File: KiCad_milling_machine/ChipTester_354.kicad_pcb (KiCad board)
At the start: 2 copper layers, 172 x 61.5 mm, 55 parts, among them U1 TLE2426xP, U2 L7805, U3 TLE2426xP, U4 TLE2426xP, U5 MCP6002-xP

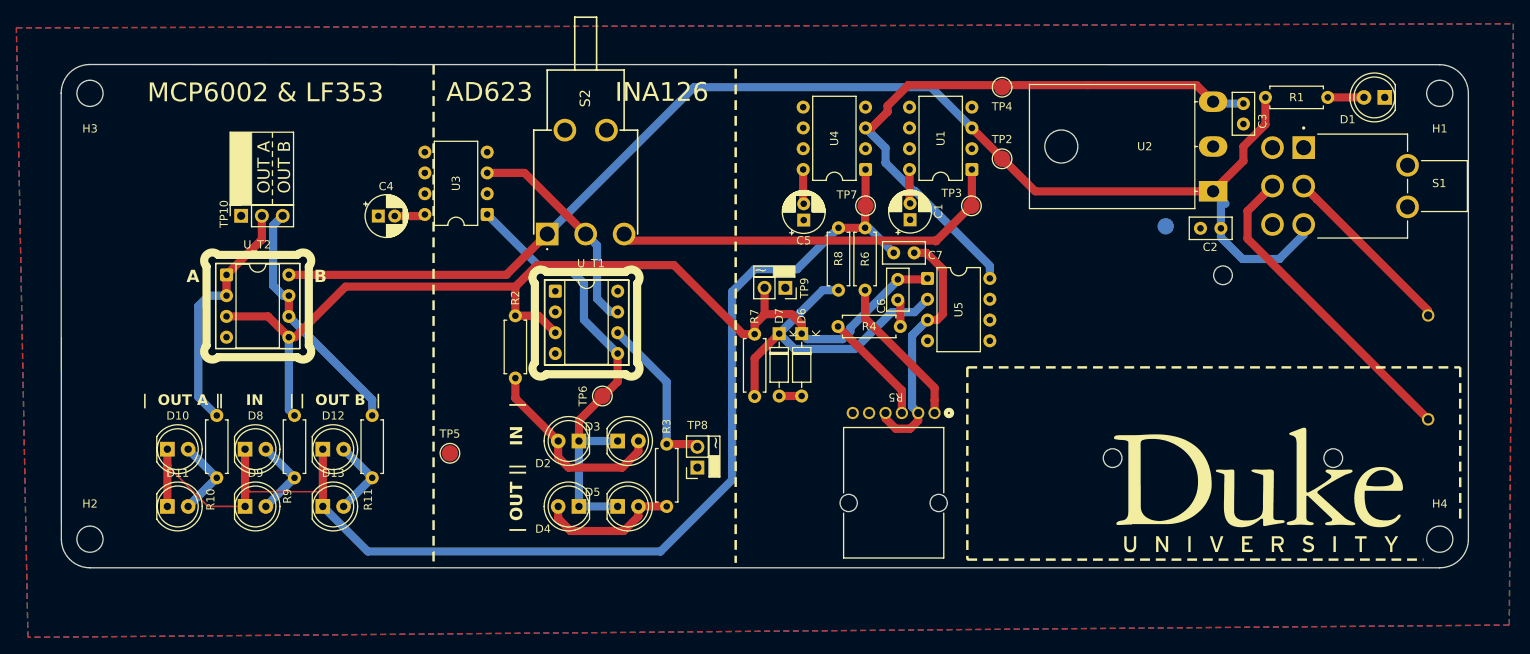
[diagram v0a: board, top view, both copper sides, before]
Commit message: Added milling machine files / updated schematic+pcb annotations /  updated footprints
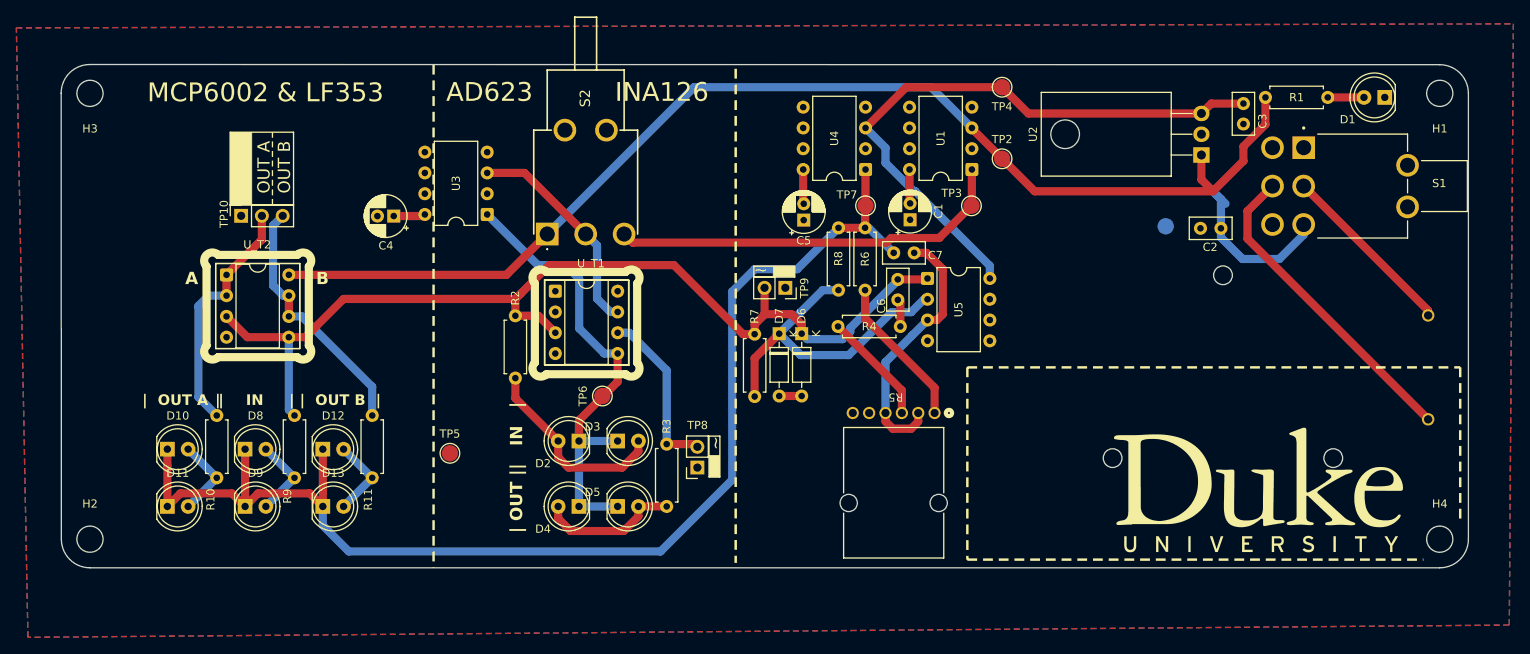
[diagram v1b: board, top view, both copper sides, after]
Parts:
- U2: footprint Package_TO_SOT_THT:TO-218-3_Horizontal_TabDown -> Package_TO_SOT_THT:TO-220-3_Horizontal_TabDown
- moved U2 4.66 mm to (204.7, 64.5)
- moved C4 1.89 mm to (106.0, 72.0), turned to 180 degrees
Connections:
- C4 pad 1: GND -> Net-(U3-NOISE_REDUCTION)
- C4 pad 2: Net-(U3-NOISE_REDUCTION) -> GND
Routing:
- net +5V: track 86.5 -> 74.9 mm
- net +9V: track 164.6 -> 168.8 mm
- net /WAVE: track 123.6 -> 121.3 mm
- net /2.5 VGND: track 152.7 -> 154.4 mm
- net /BATT+: track 24.4 -> 22.7 mm
- net Net-(R5-Pad5): track 20.1 -> 18.5 mm
- net /BATT-: track 40.4 -> 38.9 mm
- net Net-(R4-Pad2): track 15.2 -> 13.8 mm
- net /MCP6002 and IF353/MCPB_O: track 30.3 -> 31.2 mm
- net /AD623 and INA126/AD_O: track 20.0 -> 20.8 mm
- net Net-(D7-K): track 39.8 -> 40.4 mm

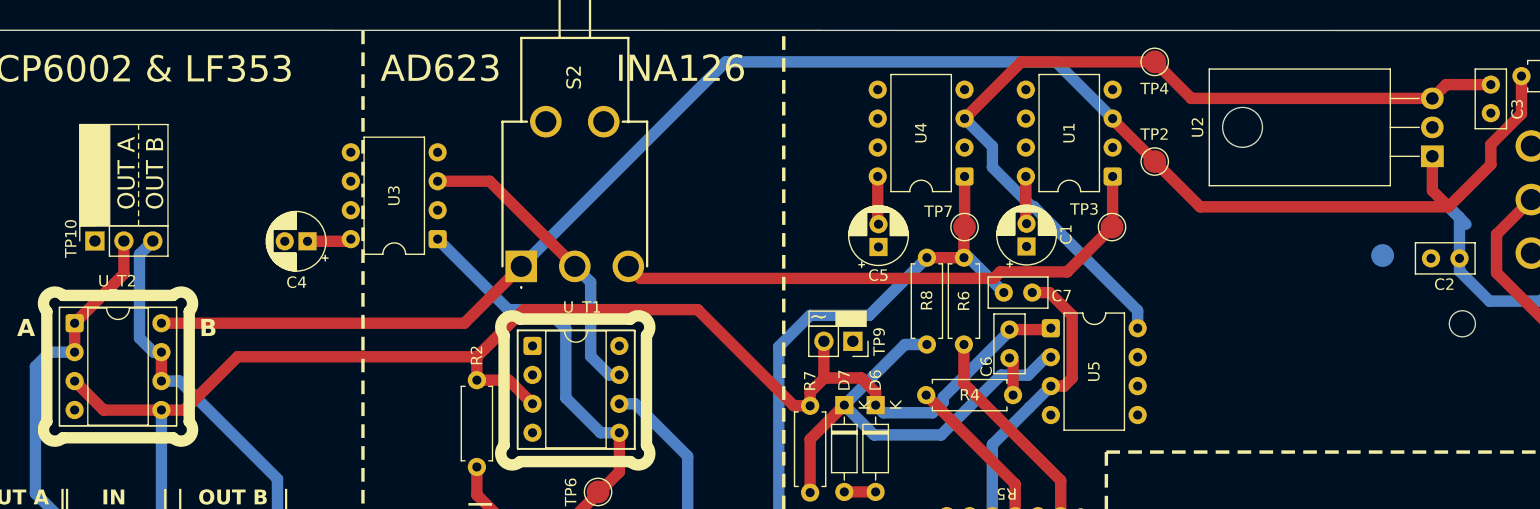
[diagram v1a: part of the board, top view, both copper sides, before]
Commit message: re-edited for 2nd milling, fixing clearances and problem areas
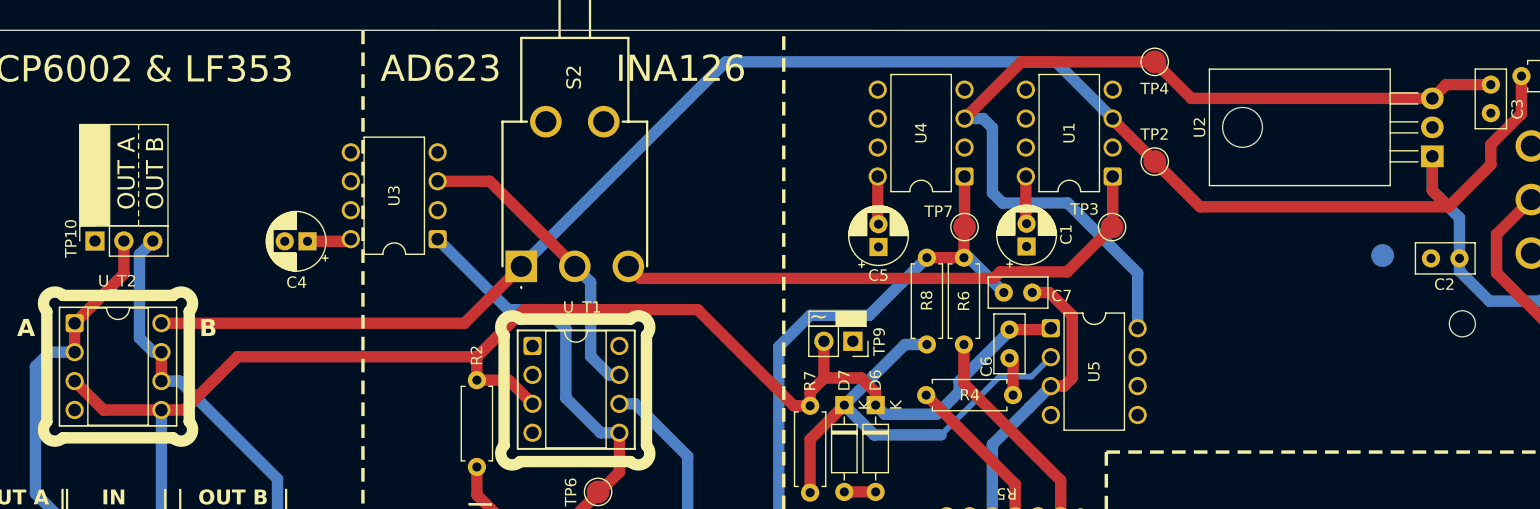
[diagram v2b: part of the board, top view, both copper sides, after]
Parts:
- C2: value 0.33 µF -> 330 pF
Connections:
- C4 pad 1: Net-(U3-NOISE_REDUCTION) -> GND
- C4 pad 2: GND -> Net-(U3-NOISE_REDUCTION)
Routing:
- net +5V: track 74.9 -> 79.1 mm
- net +9V: track 168.8 -> 171.7 mm
